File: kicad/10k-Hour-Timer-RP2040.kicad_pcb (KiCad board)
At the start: 2 copper layers, 100 x 100 mm, 179 parts, among them J1 Conn_01x03_Pin, J10 S2B-PH-K-S_LF__SN_, J11 Conn_01x02_Pin, J2 JST_SH_SM03B, J3 USB_C_Receptacle_USB2.0_16P, J4 S2B-PH-K-S_LF__SN_, J5 Conn_02x05_Counter_Clockwise, J6 Conn_02x08_Counter_Clockwise, J7 Conn_01x03_Pin, J8 Conn_01x03_Pin, J9 Conn_01x02_Pin, Q1 PMOS, Q2 AO3400A, Q3 AO3400A, Q4 AO3400A, Q5 AO3400A, Q6 PMOS, Q7 AO3400A, Q8 AO3400A, SW2 BOOTSEL, SW3 RESET, SW4 USER_A, SW5 USER_B_PWR, SW6 SW_SPDT, U10 TM1638, U2 MCP73831-2-OT, U3 BQ29700DSER, U4 TLV62568DBVR, U5 W25Q128JVS, U6 RP2040, U7 PCF8523T, U8 FJ2481CH, U9 FJ2481CH, Y1 ABM8-272-T3, Y2 ABS07AIG-32.768KHZ-7-T

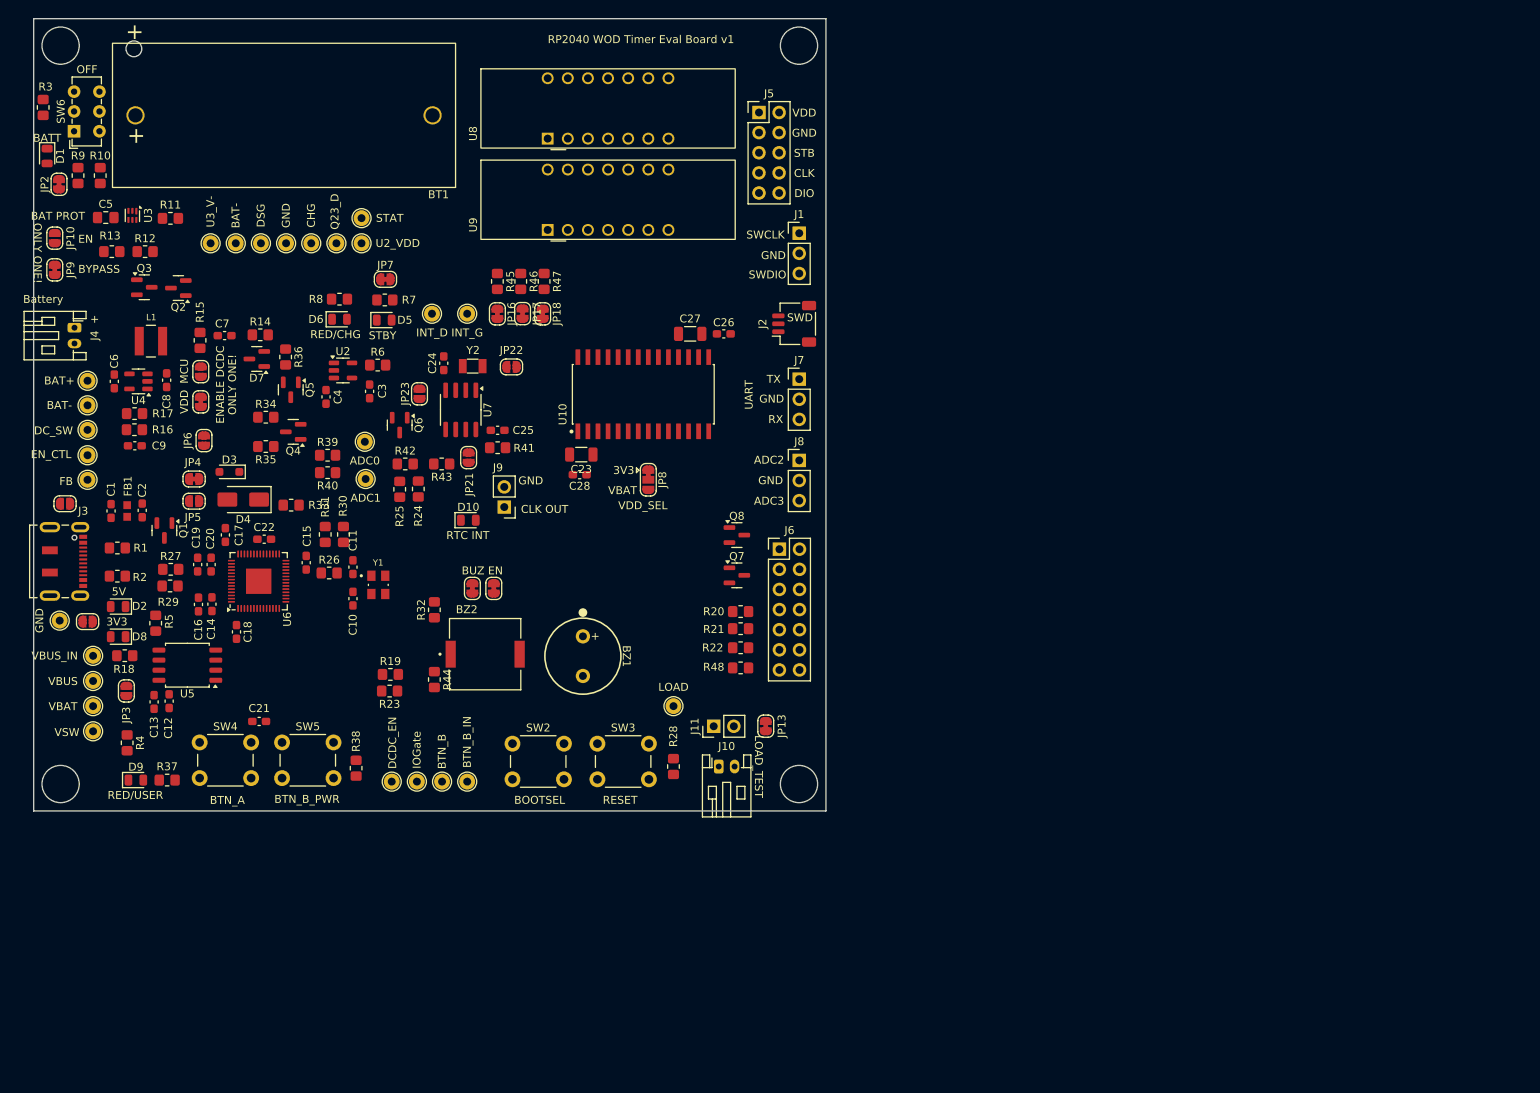
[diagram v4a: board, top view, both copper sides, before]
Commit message: start routing diff pairs
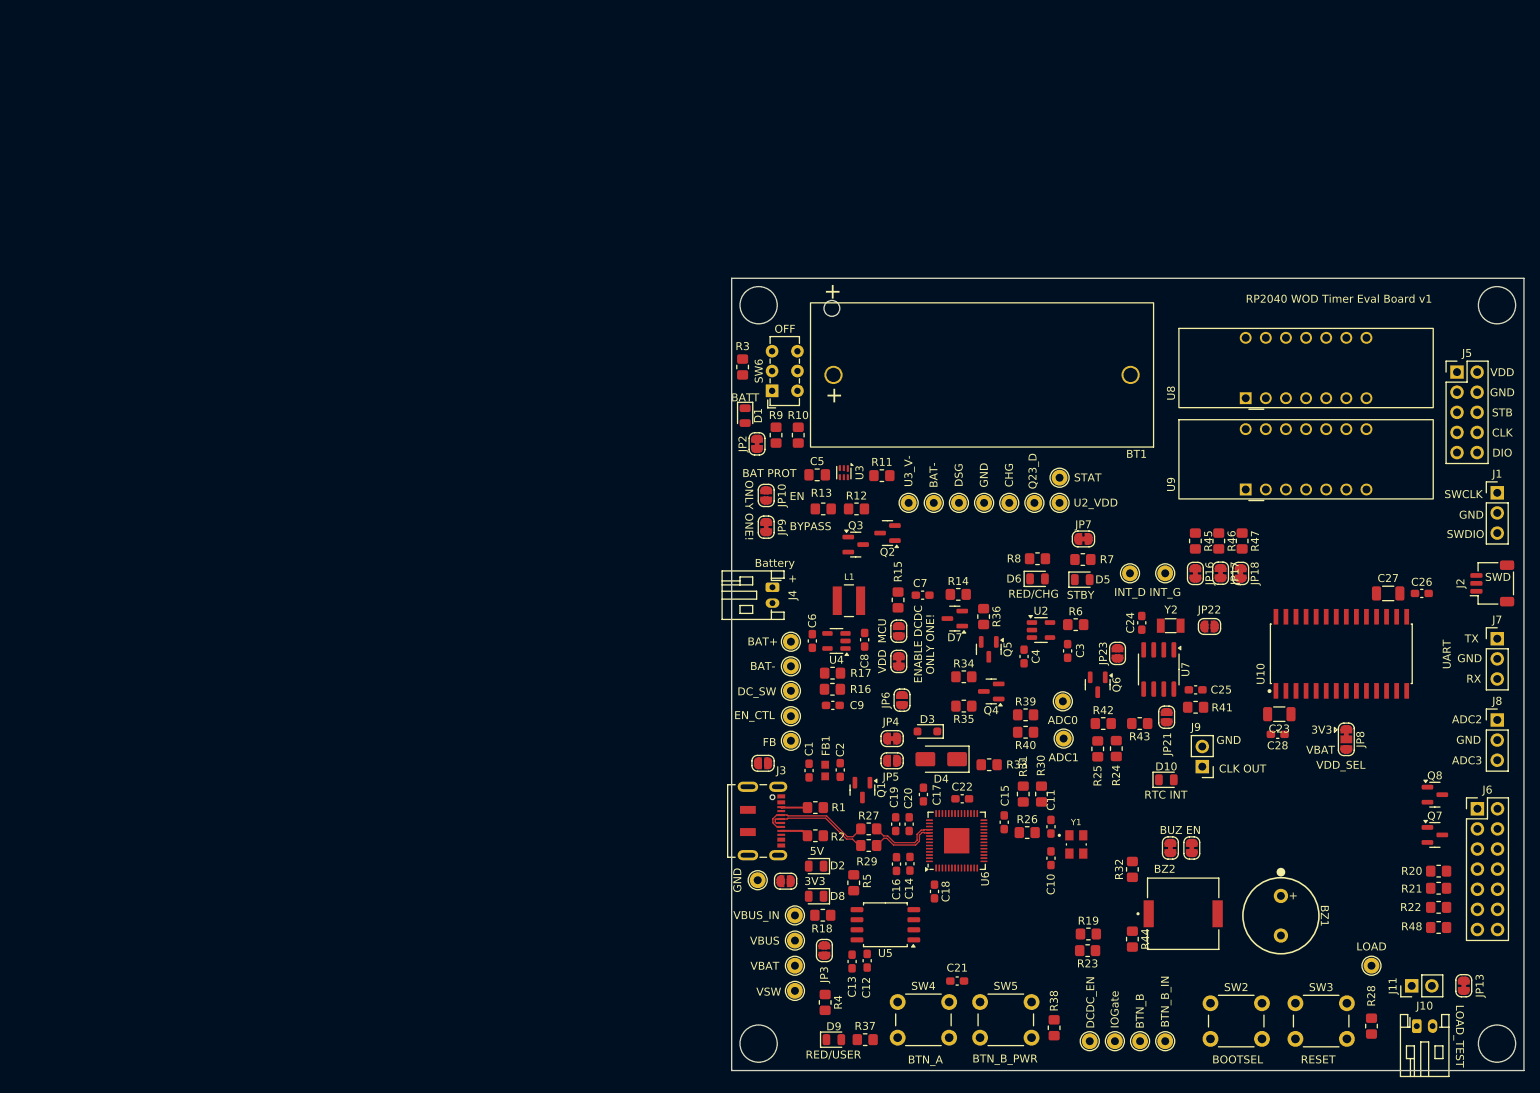
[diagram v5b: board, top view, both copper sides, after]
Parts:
- moved Q3 95.5 mm to (120.2, 82.5)
- moved R11 95.5 mm to (123.5, 73.8)
- moved R12 95.5 mm to (120.3, 78.0)
- moved U3 95.5 mm to (118.7, 73.4)
- moved C5 95.5 mm to (115.3, 73.7)
- moved JP10 95.5 mm to (108.9, 76.3)
- moved JP9 95.5 mm to (108.9, 80.3)
- moved R13 95.5 mm to (116.1, 78.0)
- moved Q2 94.7 mm to (124.2, 81.0)
- moved TP16 94.7 mm to (112.0, 104.1)
- moved TP17 94.7 mm to (112.0, 100.9)
- moved TP27 94.7 mm to (112.0, 107.2)
- moved TP8 94.7 mm to (112.0, 94.7)
- moved TP9 94.7 mm to (112.0, 97.8)
- moved TP2 94.5 mm to (112.5, 129.3)
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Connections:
- net Net-(U6-USB_DM) renamed /MCU-IO/USB_DN
- net Net-(U6-USB_DP) renamed /MCU-IO/USB_DP
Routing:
- net /USB_D-: track 0.00 -> 14.6 mm
- net /USB_D+: track 0.00 -> 13.4 mm
- net /MCU-IO/USB_DP: track 0.00 -> 8.85 mm
- net /MCU-IO/USB_DN: track 0.00 -> 8.84 mm
- net Net-(J3-CC2): track 0.00 -> 3.57 mm
- net Net-(J3-CC1): track 0.00 -> 3.34 mm
- added copper zone on In1.Cu, net GND
- added copper zone on In2.Cu, net GND
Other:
- copper layers 2 -> 4

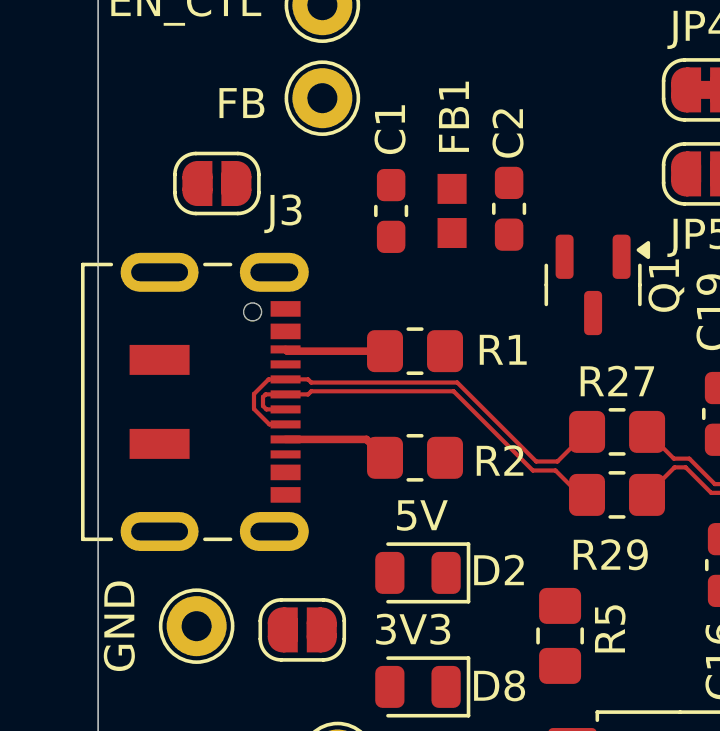
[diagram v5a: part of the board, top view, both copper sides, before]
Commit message: changed usb port, prepare first bom export
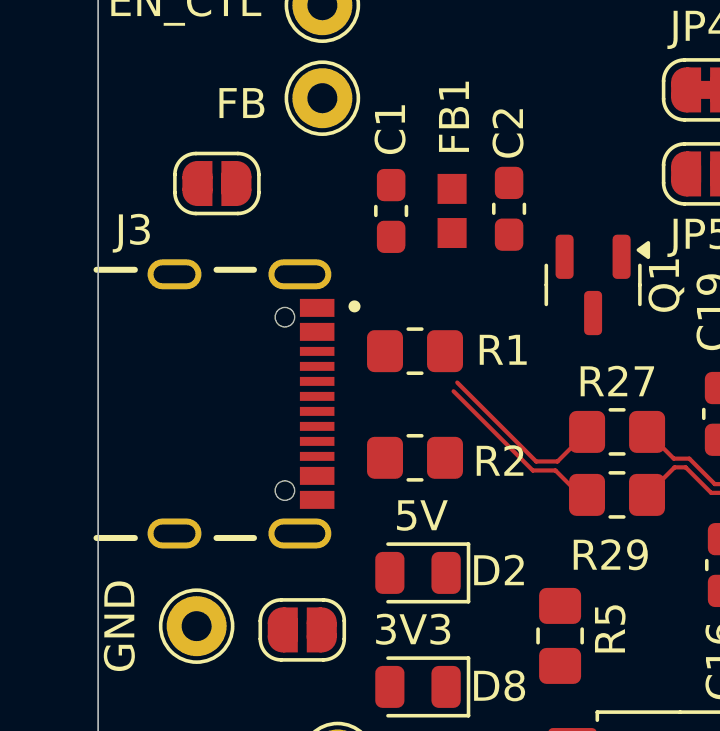
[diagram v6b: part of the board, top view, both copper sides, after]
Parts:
- J3: value USB_C_Receptacle_USB2.0_16P -> USB4105-GF-A; footprint project footprints:USB_C_Receptacle_JAE_DX07S016JA1R1500 -> project footprints:GCT_USB4105-GF-A
- moved J3 0.66 mm to (107.0, 117.4)
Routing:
- net /USB_D-: track 14.6 -> 5.83 mm
- net /USB_D+: track 13.4 -> 5.88 mm
- net Net-(J3-CC2): track 3.57 -> 0.00 mm
- net Net-(J3-CC1): track 3.34 -> 0.00 mm

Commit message: routing - power
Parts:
- moved C9 13.8 mm to (124.8, 91.3), turned to -90 degrees
- moved R16 11.0 mm to (122.9, 91.3), turned to -90 degrees
- moved R17 6.57 mm to (122.8, 95.2), turned to -90 degrees
- moved C8 6.44 mm to (119.8, 88.2), turned to 0 degrees
- moved C6 4.95 mm to (119.6, 94.5), turned to 0 degrees
- moved L1 4.43 mm to (115.3, 91.5), turned to 90 degrees
- moved U4 3.86 mm to (119.9, 91.4), turned to -90 degrees
- moved D7 2.17 mm to (134.8, 92.0)
- moved R14 2.17 mm to (135.3, 88.9)
- moved R15 1.92 mm to (126.7, 90.9)
- moved Q5 1.88 mm to (138.8, 95.8)
- moved R36 1.88 mm to (138.2, 91.7)
- moved JP12 1.78 mm to (126.6, 94.9)
- moved JP11 1.58 mm to (126.6, 98.4)
- moved C7 1.57 mm to (130.2, 88.9)
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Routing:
- net /MCU-IO/QSPI_CLK: track 0.00 -> 18.7 mm, vias 0 -> 2
- net /MCU-IO/QSPI_SD0: track 0.00 -> 16.7 mm, vias 0 -> 2
- net /MCU-IO/QSPI_SD3: track 0.00 -> 16.0 mm, vias 0 -> 2
- net /MCU-IO/VBAT_VBUS: track 0.00 -> 14.4 mm
- net /MCU-IO/HSE_IN: track 0.00 -> 14.0 mm
- net /MCU-IO/QSPI_SS: track 0.00 -> 13.7 mm, vias 0 -> 2
- net 3V3: track 0.00 -> 12.7 mm, vias 0 -> 4
- net /MCU-IO/ADC1_VSW_In: track 0.00 -> 12.4 mm
- net /MCU-IO/QSPI_SD1: track 0.00 -> 12.3 mm, vias 0 -> 2
- net /MCU-IO/QSPI_SD2: track 0.00 -> 11.0 mm, vias 0 -> 2
- net Net-(JP11-A): track 0.00 -> 9.87 mm, vias 0 -> 2
- net /USB_D+: track 5.88 -> 13.5 mm
- net /USB_D-: track 5.83 -> 12.5 mm
- net 1V1: track 0.00 -> 6.13 mm
- net /MCU-IO/HSE_OUT: track 0.00 -> 4.98 mm
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- added copper zone on F.Cu, net /MCU-IO/ADC0_VUSB_In
- added copper zone on F.Cu, net /MCU-IO/ADC1_VSW_In
- added copper zone on F.Cu, net /VBUS_IN
- added copper zone on In1.Cu, net 3V3

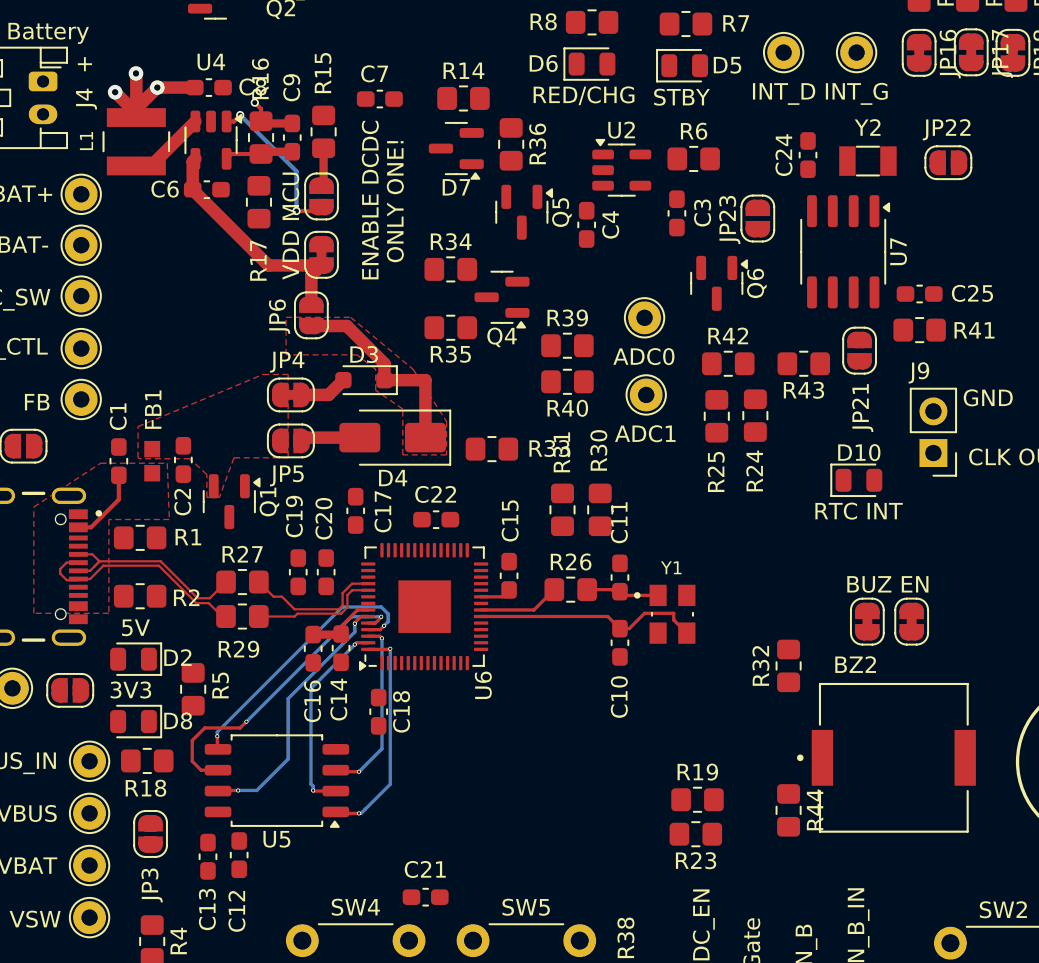
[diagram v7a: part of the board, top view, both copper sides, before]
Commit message: routing - 3v3 net
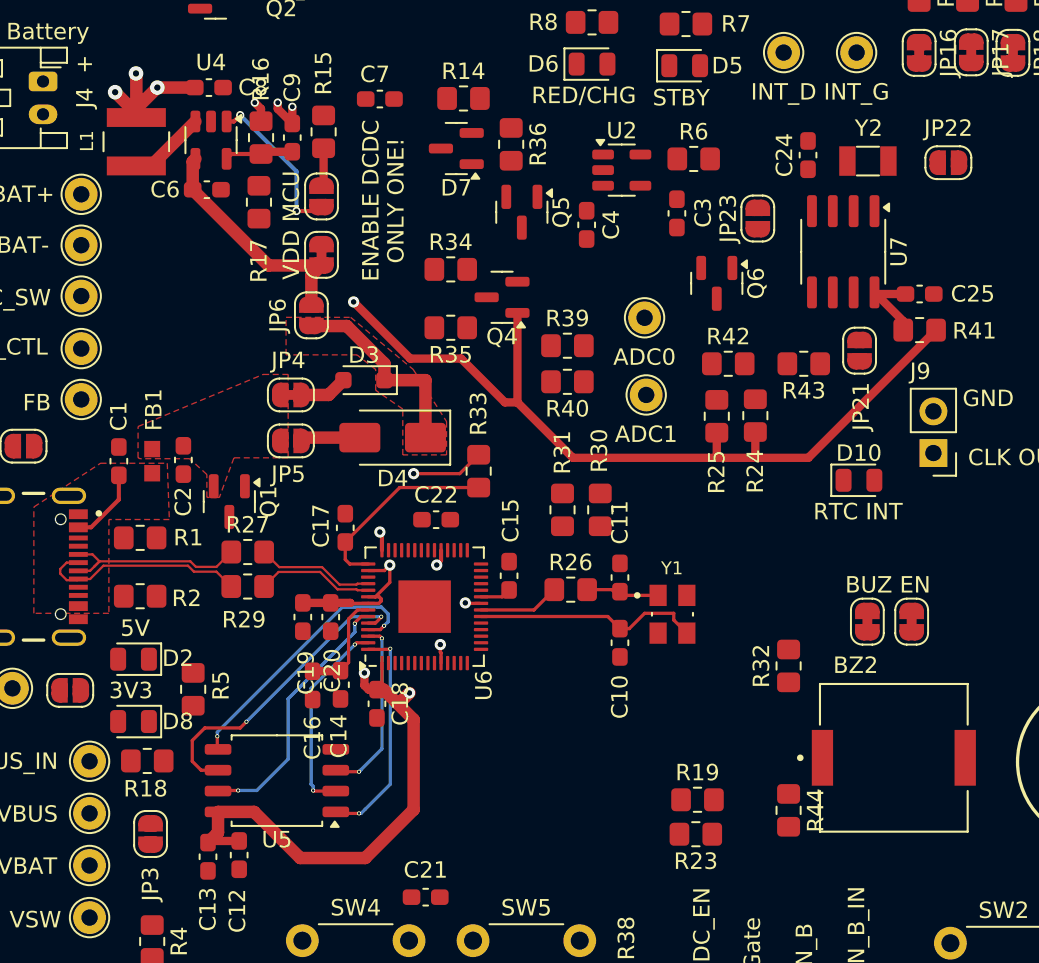
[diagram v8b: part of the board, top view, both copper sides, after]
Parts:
- moved C19 2.75 mm to (125.5, 120.5), turned to -90 degrees
- moved C20 2.75 mm to (127.2, 120.5), turned to -90 degrees
- moved C14 2.23 mm to (127.8, 124.6)
- moved C16 2.23 mm to (126.1, 124.7)
- moved R27 1.86 mm to (122.1, 116.5)
- moved R29 1.86 mm to (122.1, 118.6)
- moved R33 1.57 mm to (136.2, 111.6), turned to 90 degrees
- moved C17 1.22 mm to (128.1, 115.1)
- moved C18 0.49 mm to (130.0, 125.8)
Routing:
- net 3V3: track 12.7 -> 132.7 mm, vias 4 -> 15
- net /MCU-IO/AVDD: track 0.00 -> 12.1 mm
- net /RTC/VDD_IN: track 0.00 -> 4.95 mm
- net 1V1: track 6.13 -> 8.38 mm
- net /MCU-IO/USB_DN: track 8.43 -> 7.19 mm
- net /MCU-IO/USB_DP: track 7.77 -> 7.18 mm
- net /USB_D-: track 12.5 -> 12.0 mm
- added copper zone on In2.Cu, net 3V3
- removed copper zone on In1.Cu, net 3V3
